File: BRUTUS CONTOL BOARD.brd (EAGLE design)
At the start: 110.5 x 86.4 mm, 42 parts, among them IC1 ATMEGA168PROUND, IC4 74LS595N, IC5 74LS595N, IC6 4021N, IC7 4021N, IC8 74LS14N, Q1 16MHz, X1 5566-16, X2 5566-16, X3 5566-2, X4 5566-6, X5 5566-6, X6 5566-8, X7 5566-4

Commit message: rev1
second commit
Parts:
- removed IC7: 4021N, 40xx:DIL16
- removed IC8: 74LS14N, 74xx-us:DIL14
- removed R22: 10k, adafruit:0204V
- added IC2, IC3: 74LS595N, 74xx-us:DIL16
- added R14: 10k, adafruit:0204V
- C1, C2: value 22uF -> 10uF
- C4, C5: value 10uF -> 22uF
- IC1: value ATMEGA168PROUND -> 74LS14N; device adafruit:DIL28-3-ROUND -> 74xx-us:DIL14
- IC4: value 74LS595N -> ATMEGA168PROUND; device 74xx-us:DIL16 -> adafruit:DIL28-3-ROUND
- IC5: value 74LS595N -> 4021N; device 74xx-us:DIL16 -> 40xx:DIL16
- R2: value 10k -> 220
- R3: value 220 -> 10k
- X1: value 5566-16 -> 5566-6; device con-molex:5566-16 -> con-molex:5566-6
- X4: value 5566-6 -> 5566-4; device con-molex:5566-6 -> con-molex:5566-4
- X5: value 5566-6 -> 5566-16; device con-molex:5566-6 -> con-molex:5566-16
- X7: value 5566-4 -> 5566-6; device con-molex:5566-4 -> con-molex:5566-6
- moved X1 84.9 mm to (96.5, 53.3)
- moved X5 84.9 mm to (24.1, 8.89)
- moved C1 80.5 mm to (99.1, 78.7), turned to 0 degrees
- moved C2 66.8 mm to (99.1, 72.4)
- moved IC1 56.1 mm to (80.0, 72.4), turned to 270 degrees
- moved R13 53.3 mm to (78.7, 27.9), turned to 90 degrees
- moved R4 52.2 mm to (90.2, 67.3), turned to 0 degrees
- moved R21 52.1 mm to (78.7, 21.6), turned to 90 degrees
- moved Q1 50.6 mm to (73.7, 44.5)
- moved IC4 45.9 mm to (61.0, 55.9)
- moved R2 45.3 mm to (50.8, 72.4), turned to 180 degrees
- moved IC5 41.5 mm to (11.4, 25.4), turned to 270 degrees
- moved R3 40.7 mm to (90.2, 72.4), turned to 0 degrees
- moved R5 39.4 mm to (66.0, 64.8), turned to 0 degrees
- moved C5 38.7 mm to (83.8, 44.5)
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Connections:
- removed net DIGPIN9: IC1.15, IC8.8
- new net DIGPIN10: IC1.8, IC4.16
- net ANLG1: now also IC4.24, X7.3; no longer IC1.24, X4.3
- net ANLG2: now also IC4.25, X7.4; no longer IC1.25, X4.4
- net ANLG3: now also IC4.26, X7.5; no longer IC1.26, X4.5
- net DIGPIN11: now also IC4.17, IC5.9; no longer IC1.17, IC7.9
- net DIGPIN12: now also IC4.18, IC5.10; no longer IC1.18, IC7.10
- net DIGPIN2: now also IC1.10, IC4.4; no longer IC1.4, IC8.10
- net DIGPIN3: now also IC1.12, IC4.5; no longer IC1.5, IC8.12
- net DIGPIN4: now also IC2.14, IC4.6; no longer IC1.6, IC4.14
- net DIGPIN5: now also IC2.12, IC3.12, IC4.11; no longer IC1.11, IC4.12, IC5.12
- net DIGPIN6: now also IC2.11, IC3.11, IC4.12; no longer IC1.12, IC4.11, IC5.11
- net DIGPIN7: now also IC4.13, IC5.3; no longer IC1.13, IC6.3
- net GND: now also C3.1, C4.2, IC1.7, IC2.13, IC2.8, IC3.13, IC3.8, IC4.22, R2.2, X1.2, X1.4, X4.4, X7.6; no longer C3.2, C4.1, IC1.22, IC1.8, IC4.13, IC5.13, IC5.8, IC8.7, R3.2, X4.6, X5.2, X5.4, X7.4
- net IC8A: now also C1.1, IC1.13, R1.2, X1.1; no longer C5.1, IC8.13, R13.2, X5.1
- net IC8B: now also C2.1, IC1.11, R3.2, X1.3; no longer C3.1, IC8.11, R21.2, X5.3
- net IC8C: now also C3.2, IC1.9, R4.2, X1.5; no longer C4.2, IC8.9, R22.2, X5.5
- net N$1: now also C4.1, IC4.9; no longer C1.1, IC1.9
- net N$17: now also IC5.11, IC6.3; no longer IC6.11, IC7.3
- net N$2: now also C5.1, IC4.10; no longer C2.1, IC1.10
- net N$3: now also IC4.1, R5.2; no longer IC1.1, R1.2
- net N$5: now also IC4.19; no longer IC1.19
- net N$6: now also R2.1; no longer R3.1
- net N$7: now also IC2.9, IC3.14; no longer IC4.9, IC5.14
- net SCL: now also IC4.28, X4.3; no longer IC1.28, X7.3
- net SDA: now also IC4.27, X4.2; no longer IC1.27, X7.2
- net VCC: now also IC1.14, IC2.16, IC3.10, IC3.16, IC4.20, IC4.21, IC4.7, R13.2, R14.1, R17.1, R18.1, R19.1, R21.2, R6.2, R7.2, R9.1; no longer IC1.20, IC1.21, IC1.7, IC4.16, IC5.10, IC5.16, IC8.14, R13.1, R17.2, R18.2, R19.2, R2.1, R22.1, R6.1, R7.1, R9.2
- net VDD: now also IC5.16; no longer IC7.16
- net VSS: now also IC5.8; no longer IC7.8
- net X1-1: now also IC5.7, R16.2, X5.1; no longer IC6.7, R2.2, X1.1
- net X1-10: now also IC6.6, R21.1, X5.10; no longer IC7.6, R10.1, X1.10
- net X1-11: now also IC6.5, R7.1, X5.11; no longer IC7.5, R12.1, X1.11
- net X1-12: now also IC6.4, R6.1, X5.12; no longer IC7.4, R11.1, X1.12
- net X1-13: now also R11.1, X5.13; no longer R18.1, X1.13
- net X1-14: now also IC6.14, R10.1, X5.14; no longer IC7.14, R17.1, X1.14
- net X1-15: now also IC6.15, R12.1, X5.15; no longer IC7.15, R19.1, X1.15
- net X1-16: now also IC6.1, R13.1, X5.16; no longer IC7.1, R20.1, X1.16
- net X1-2: now also IC5.6, R15.2, X5.2; no longer IC6.6, R4.2, X1.2
- net X1-3: now also IC5.5, R14.2, X5.3; no longer IC6.5, R5.2, X1.3
- net X1-4: now also IC5.4, R17.2, X5.4; no longer IC6.4, R6.2, X1.4
- net X1-5: now also IC5.13, R18.2, X5.5; no longer IC6.13, R7.2, X1.5
- net X1-6: now also IC5.14, R8.2, X5.6; no longer IC6.14, R15.2, X1.6
- net X1-7: now also IC5.15, R19.2, X5.7; no longer IC6.15, R8.2, X1.7
- net X1-8: now also IC5.1, R9.2, X5.8; no longer IC6.1, R16.2, X1.8
- net X1-9: now also IC6.7, R20.1, X5.9; no longer IC7.7, R9.1, X1.9
- net X2-1: now also IC2.15; no longer IC4.15
- net X2-10: now also IC3.1; no longer IC5.1
- net X2-11: now also IC3.2; no longer IC5.2
- net X2-12: now also IC3.3; no longer IC5.3
- net X2-13: now also IC3.4; no longer IC5.4
- net X2-14: now also IC3.5; no longer IC5.5
- net X2-15: now also IC3.6; no longer IC5.6
- net X2-16: now also IC3.7; no longer IC5.7
- net X2-2: now also IC2.1; no longer IC4.1
- net X2-3: now also IC2.2; no longer IC4.2
- net X2-4: now also IC2.3; no longer IC4.3
- net X2-5: now also IC2.4; no longer IC4.4
- net X2-6: now also IC2.5; no longer IC4.5
- net X2-7: now also IC2.6; no longer IC4.6
- net X2-8: now also IC2.7; no longer IC4.7
- net X2-9: now also IC3.15; no longer IC5.15
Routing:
- net X1-7: track 207.1 -> 104.6 mm, vias 2 -> 1
- net X2-16: track 92.1 -> 21.6 mm, vias 2 -> 0
- net X1-15: track 92.6 -> 156.1 mm, vias 3 -> 2
- net DIGPIN4: track 21.5 -> 84.4 mm
- net DIGPIN9: track 59.3 -> 0.00 mm, vias 1 -> 0
- net DIGPIN3: track 97.8 -> 51.3 mm, vias 4 -> 1
- net N$3: track 92.4 -> 49.6 mm
- net X1-16: track 77.0 -> 118.4 mm, vias 0 -> 1
- net ANLG2: track 149.6 -> 109.3 mm, vias 2 -> 4
- net ANLG1: track 137.2 -> 99.5 mm, vias 2 -> 4
- net DIGPIN2: track 84.1 -> 47.3 mm, vias 3 -> 1
- net X1-6: track 108.4 -> 76.1 mm
- net DIGPIN6: track 55.5 -> 86.4 mm
- net X2-15: track 62.3 -> 31.7 mm, vias 4 -> 0
- net X2-4: track 33.7 -> 62.6 mm
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
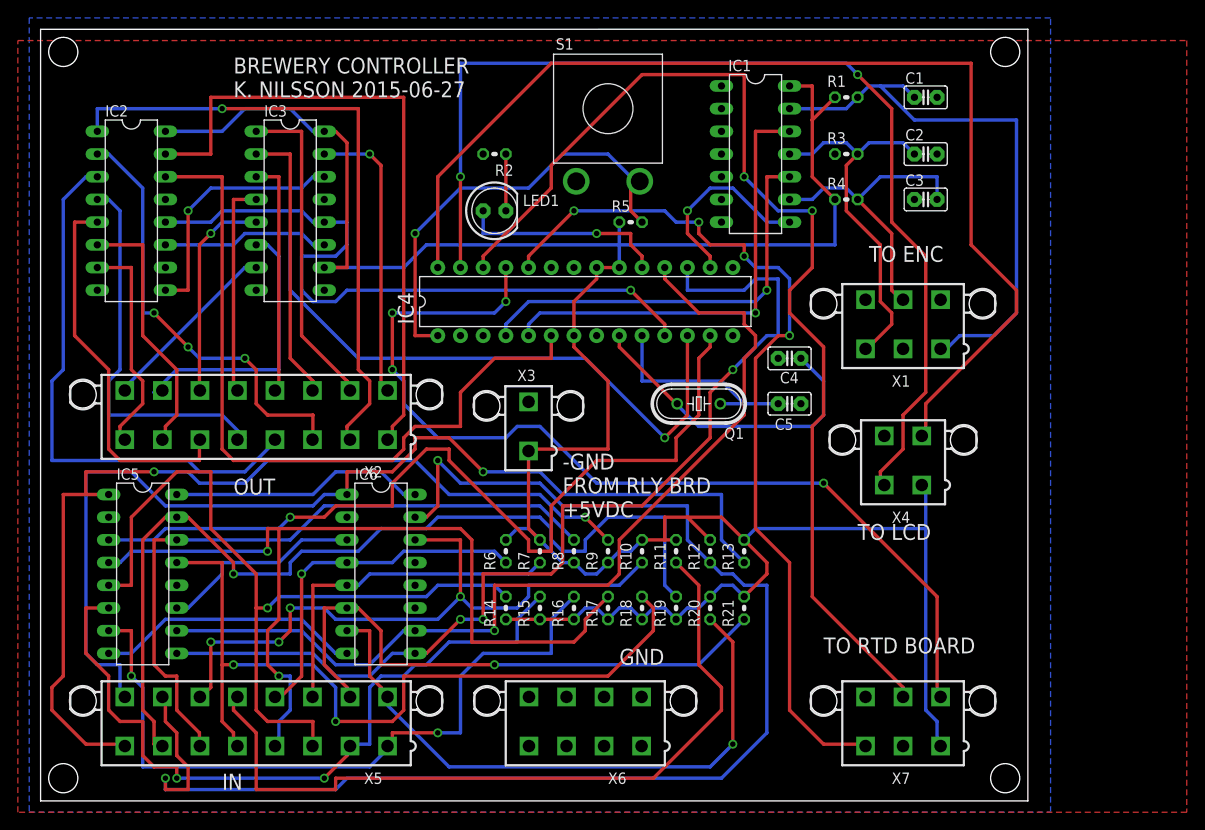
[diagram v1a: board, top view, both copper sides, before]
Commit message: REV 2
Changed to IC socket for ATmega328 connection
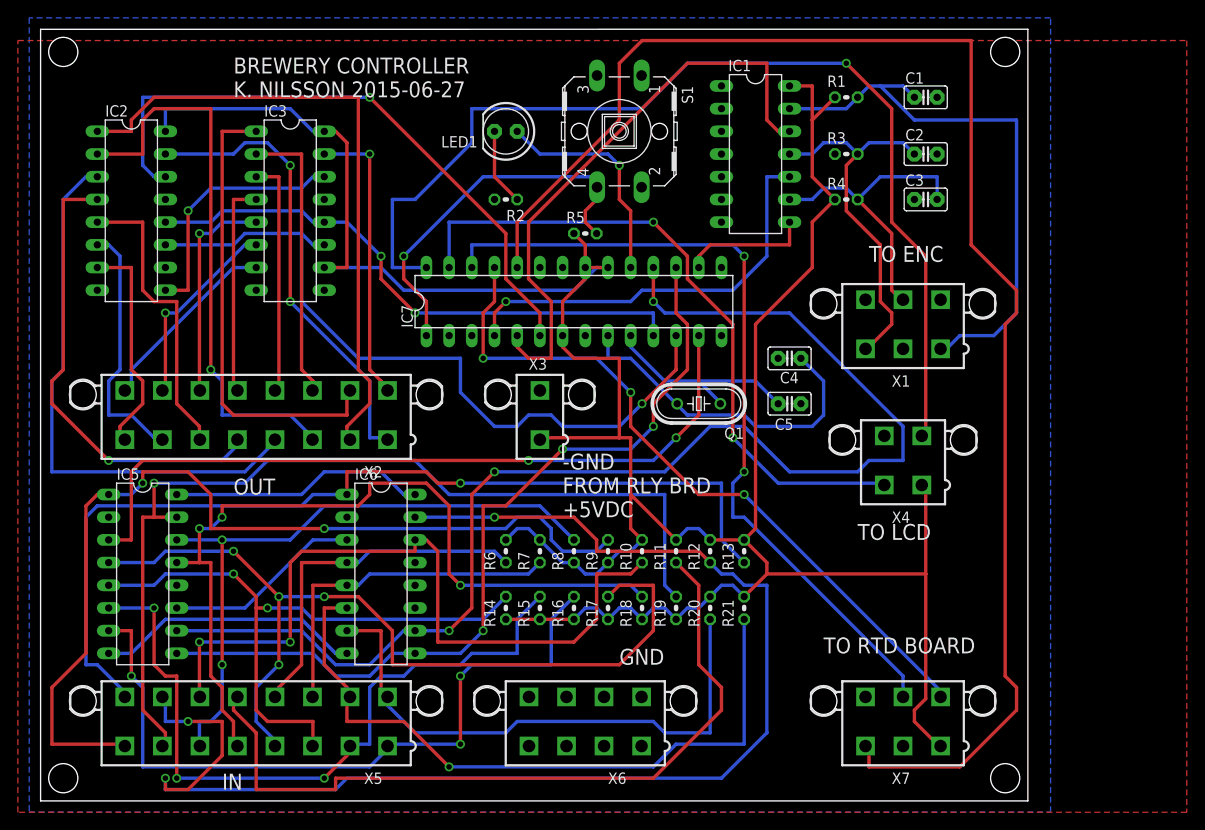
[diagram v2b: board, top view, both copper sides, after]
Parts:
- removed IC4: ATMEGA168PROUND, adafruit:DIL28-3-ROUND
- added IC7: (no value), ic-package:DIL28-3
- S1: value SPST -> (none); device adafruit:JUDCOSPST -> adafruit:B3F-40XX
- moved LED1 8.98 mm to (52.1, 74.9), turned to 180 degrees
- moved R5 5.24 mm to (61.0, 63.5)
- moved R2 5.24 mm to (52.1, 67.3)
- moved S1 2.84 mm to (64.8, 74.9), turned to 270 degrees
- moved X3 1.80 mm to (55.9, 43.2)
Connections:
- removed net N$1: C4.1, IC4.9, Q1.2
- removed net N$2: C5.1, IC4.10, Q1.1
- removed net N$3: IC4.1, R5.2, S1.P
- removed net N$5: IC4.19, LED1.A
- new net CLK10: C5.1, IC7.10, Q1.1
- new net CLK9: C4.1, IC7.9, Q1.2
- new net DIGPIN13: IC7.19, LED1.A
- new net RESET: IC7.1, R5.2, S1.4
- net ANLG1: now also IC7.24; no longer IC4.24
- net ANLG2: now also IC7.25; no longer IC4.25
- net ANLG3: now also IC7.26; no longer IC4.26
- net DIGPIN10: now also IC7.16; no longer IC4.16
- net DIGPIN11: now also IC7.17; no longer IC4.17
- net DIGPIN12: now also IC7.18; no longer IC4.18
- net DIGPIN2: now also IC7.4; no longer IC4.4
- net DIGPIN3: now also IC7.5; no longer IC4.5
- net DIGPIN4: now also IC7.6; no longer IC4.6
- net DIGPIN5: now also IC7.11; no longer IC4.11
- net DIGPIN6: now also IC7.12; no longer IC4.12
- net DIGPIN7: now also IC7.13; no longer IC4.13
- net GND: now also IC7.22, IC7.8, S1.2; no longer IC4.22, IC4.8, S1.T
- net SCL: now also IC7.28; no longer IC4.28
- net SDA: now also IC7.27; no longer IC4.27
- net VCC: now also IC7.20, IC7.21, IC7.7; no longer IC4.20, IC4.21, IC4.7
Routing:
- net ANLG1: track 99.5 -> 168.2 mm, vias 4 -> 0
- net N$3: track 49.6 -> 0.00 mm, vias 1 -> 0
- net SDA: track 119.3 -> 74.9 mm
- net RESET: track 0.00 -> 42.6 mm, vias 0 -> 1
- net DIGPIN12: track 106.1 -> 145.3 mm, vias 1 -> 3
- net CLK9: track 0.00 -> 37.9 mm
- net N$1: track 36.0 -> 0.00 mm
- net ANLG3: track 123.0 -> 92.2 mm
- net ANLG2: track 109.3 -> 81.7 mm, vias 4 -> 3
- net DIGPIN13: track 0.00 -> 25.0 mm, vias 0 -> 1
- net CLK10: track 0.00 -> 24.1 mm
- net N$2: track 24.0 -> 0.00 mm
- net N$5: track 23.4 -> 0.00 mm, vias 1 -> 0
- net X2-1: track 72.2 -> 51.7 mm, vias 0 -> 2
- net DIGPIN11: track 113.4 -> 94.0 mm
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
